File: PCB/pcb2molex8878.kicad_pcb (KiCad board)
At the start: 2 copper layers, 16.2 x 38 mm, 1 part

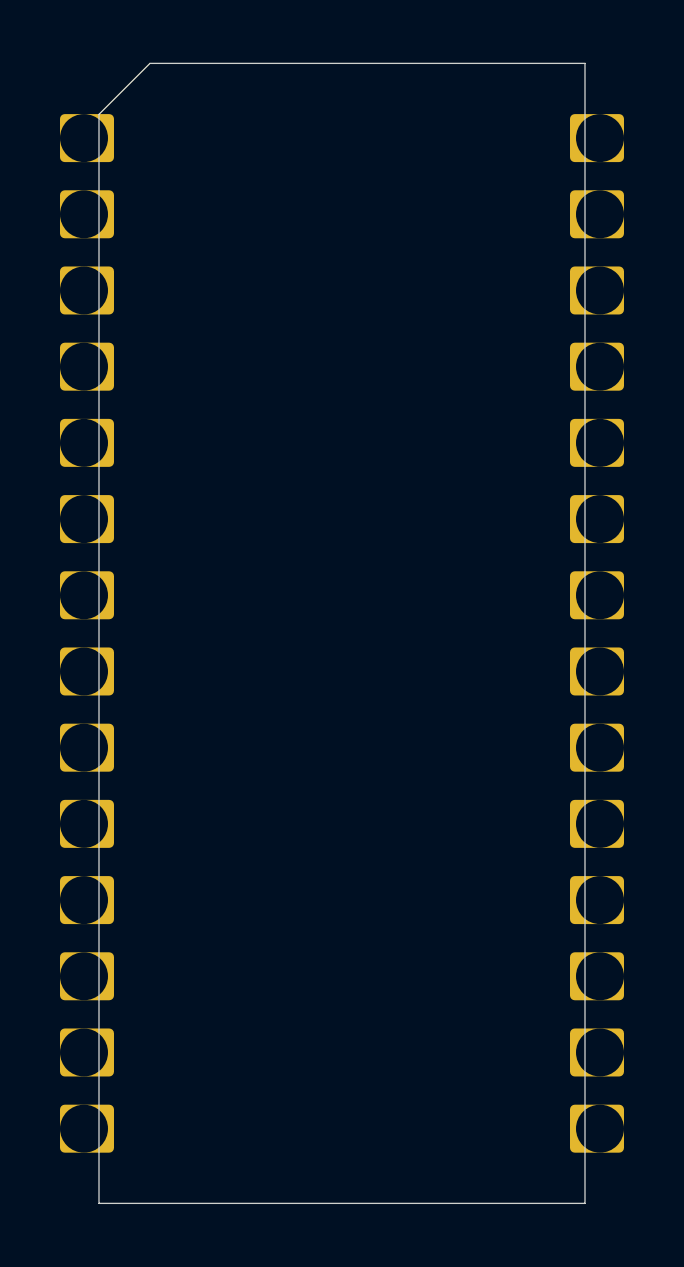
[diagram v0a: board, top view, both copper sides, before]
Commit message: update pcb to match carrier
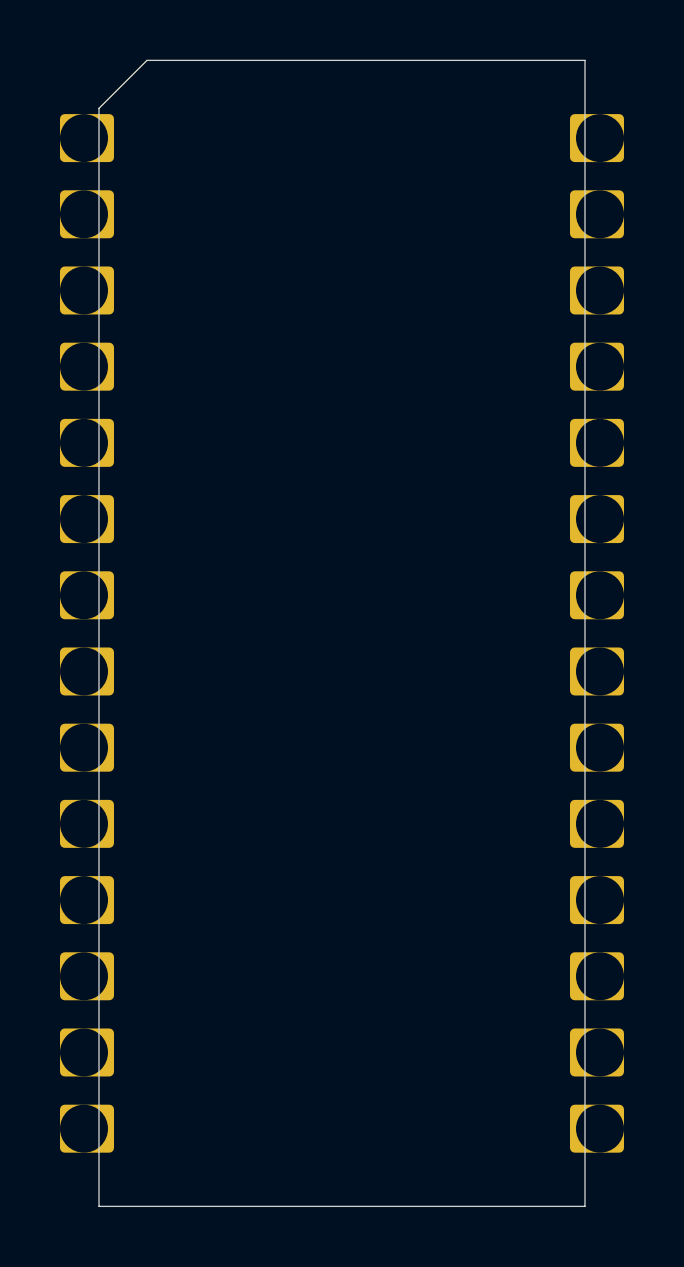
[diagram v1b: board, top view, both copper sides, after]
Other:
- board size 16.2 x 38 mm -> 16.2 x 38.2 mm

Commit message: desperate measures to get a little more bite on the corners. create makefile to generate stls
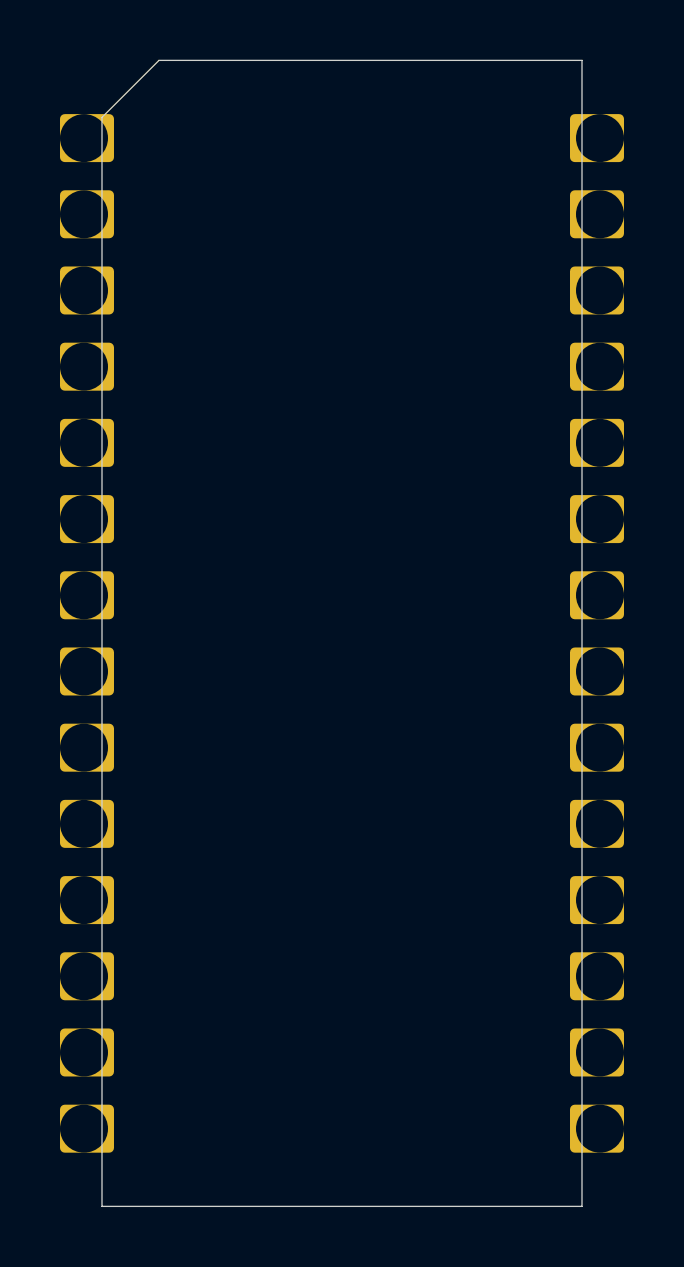
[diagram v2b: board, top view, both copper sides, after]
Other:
- board size 16.2 x 38.2 mm -> 16 x 38.2 mm
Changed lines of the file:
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@@
     (41 Cmts.User user hide)
     (42 Eco1.User user hide)
-    (43 Eco2.User user hide)
+    (43 Eco2.User user)
     (44 Edge.Cuts user)
     (45 Margin user hide)
@@
       (effects (font (size 1.2065 1.2065) (thickness 0.1016)) (justify left bottom))
     )
+    (fp_line (start 8 -19.1) (end -6.3 -19.1) (layer Eco2.User) (width 0.01))
+    (fp_line (start -8 19.1) (end 8 19.1) (layer Eco2.User) (width 0.01))
     (fp_line (start -8.1 -19.1) (end 8.1 19.1) (layer Dwgs.User) (width 0.01))
     (fp_line (start -8.1 19.1) (end 8.1 -19.1) (layer Dwgs.User) (width 0.01))
-    (fp_line (start -8.1 19.1) (end -8.1 -17.4) (layer Eco2.User) (width 0.01))
-    (fp_line (start 8.1 19.1) (end 8.1 -19.1) (layer Eco2.User) (width 0.01))
+    (fp_line (start -8 19.1) (end -8 -17.4) (layer Eco2.User) (width 0.01))
+    (fp_line (start 8 19.1) (end 8 -19.1) (layer Eco2.User) (width 0.01))
     (fp_line (start -0.762 -19.05) (end -0.762 -21.59) (layer Eco1.User) (width 0.01))
     (fp_line (start -0.762 -21.59) (end 0.762 -21.59) (layer Eco1.User) (width 0.01))
@@
       (effects (font (size 0.2 0.2) (thickness 0.01)))
     )
-    (fp_line (start -8.1 19.1) (end 8.1 19.1) (layer Eco2.User) (width 0.01))
     (fp_line (start -6.25 18) (end 6.25 18) (layer Dwgs.User) (width 0.01))
     (fp_line (start 6.25 18) (end 6.25 -18) (layer Dwgs.User) (width 0.01))
@@
     (fp_line (start -8.1 19.05) (end -4.5593 19.05) (layer Eco1.User) (width 0.01))
     (fp_line (start 4.5593 19.05) (end 8.1 19.05) (layer Eco1.User) (width 0.01))
-    (fp_line (start -8.1 -17.4) (end -6.4 -19.1) (layer Eco2.User) (width 0.01))
-    (fp_line (start 8.1 -19.1) (end -6.4 -19.1) (layer Eco2.User) (width 0.01))
-    (fp_line (start -6.4 -19.1) (end -8.1 -19.1) (layer Dwgs.User) (width 0.01))
-    (fp_line (start -8.1 -19.1) (end -8.1 -17.4) (layer Dwgs.User) (width 0.01))
+    (fp_line (start -8 -17.4) (end -6.3 -19.1) (layer Eco2.User) (width 0.01))
+    (fp_line (start -6.3 -19.1) (end -8 -19.1) (layer Dwgs.User) (width 0.01))
+    (fp_line (start -8 -19.1) (end -8 -17.4) (layer Dwgs.User) (width 0.01))
     (pad 28 thru_hole roundrect (at 8.6 -16.51 180) (size 1.8 1.6) (drill 1.6 (offset 0.1 0)) (layers *.Cu *.Mask) (roundrect_rratio 0.1)
       (solder_mask_margin -0.19))
@@
     )
   )
-  (gr_line (start 139.1184 81.687) (end 139.1184 118.287) (layer Edge.Cuts) (width 0.0254))
-  (gr_line (start 140.7184 80.087) (end 155.3184 80.087) (layer Edge.Cuts) (width 0.0254))
-  (gr_line (start 140.7184 80.087) (end 139.1184 81.687) (layer Edge.Cuts) (width 0.0254))
-  (gr_line (start 155.3184 118.287) (end 155.3184 80.087) (layer Edge.Cuts) (width 0.0254))
-  (gr_line (start 139.1184 118.287) (end 155.3184 118.287) (layer Edge.Cuts) (width 0.0254))
+  (gr_line (start 141.1184 80.087) (end 155.2184 80.087) (layer Edge.Cuts) (width 0.0254))
+  (gr_line (start 139.2184 118.287) (end 139.2184 81.987) (layer Edge.Cuts) (width 0.0254))
+  (gr_line (start 141.1184 80.087) (end 139.2184 81.987) (layer Edge.Cuts) (width 0.0254))
+  (gr_line (start 155.2184 118.287) (end 139.2184 118.287) (layer Edge.Cuts) (width 0.0254))
+  (gr_line (start 155.2184 118.287) (end 155.2184 80.087) (layer Edge.Cuts) (width 0.0254))
 )
